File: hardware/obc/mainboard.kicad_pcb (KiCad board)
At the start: 6 copper layers, 95.9 x 90.2 mm, 216 parts, among them J101 Conn_02x20_Odd_Even, J301 USB_C_Receptacle_USB2.0, J302 Conn_High-Rel_4S2P_Vertical, J303 Conn_01x06, J304 Conn_High-Rel_6P, J305 Conn_01x05, J601 Conn_01x08_Socket, J602 SMA RA Connector, J603 SMA RA Connector, J604 SMA RA Connector, Q201 BSS138DWQ-7, Q202 BSS138DWQ-7, Q203 MBT2222ADW1T1, Q204 MBT2222ADW1T1, Q205 BSS138DWQ-7, Q206 BSS138DWQ-7, Q207 MBT2222ADW1T1, Q208 MBT2222ADW1T1, Q209 MMDT2907, Q401 MBT2222ADW1T1, Q402 MBT2222ADW1T1, Q403 IRLML2803, Q404 IRF7406PbF, Q501 MMBT2222AT, Q502 IRLML2803, Q503 IRLML2803, Q504 IRLML2803, Q505 IRF7406PbF, Q506 IRF7406PbF, Q507 IRF7406PbF, U101 MAX706RESA, U102 ATSAMD51J20A-AU, U103 BMI088, U301 Mem_MT29F4G01ABAFDWB, U302 Mem_MT29F4G01ABAFDWB, U401 TPS7A4501DCQT, U402 LTC4121, U403 TPS54226PWPRPWP14_2P31X2P46-L, U404 ADM1176-1ARMZ-R7, U405 BQ25886RGER, U501 PE014006, U601 RFM98PW, U602 S1216V8, U603 GP2S1+, Y101 32.768kHz

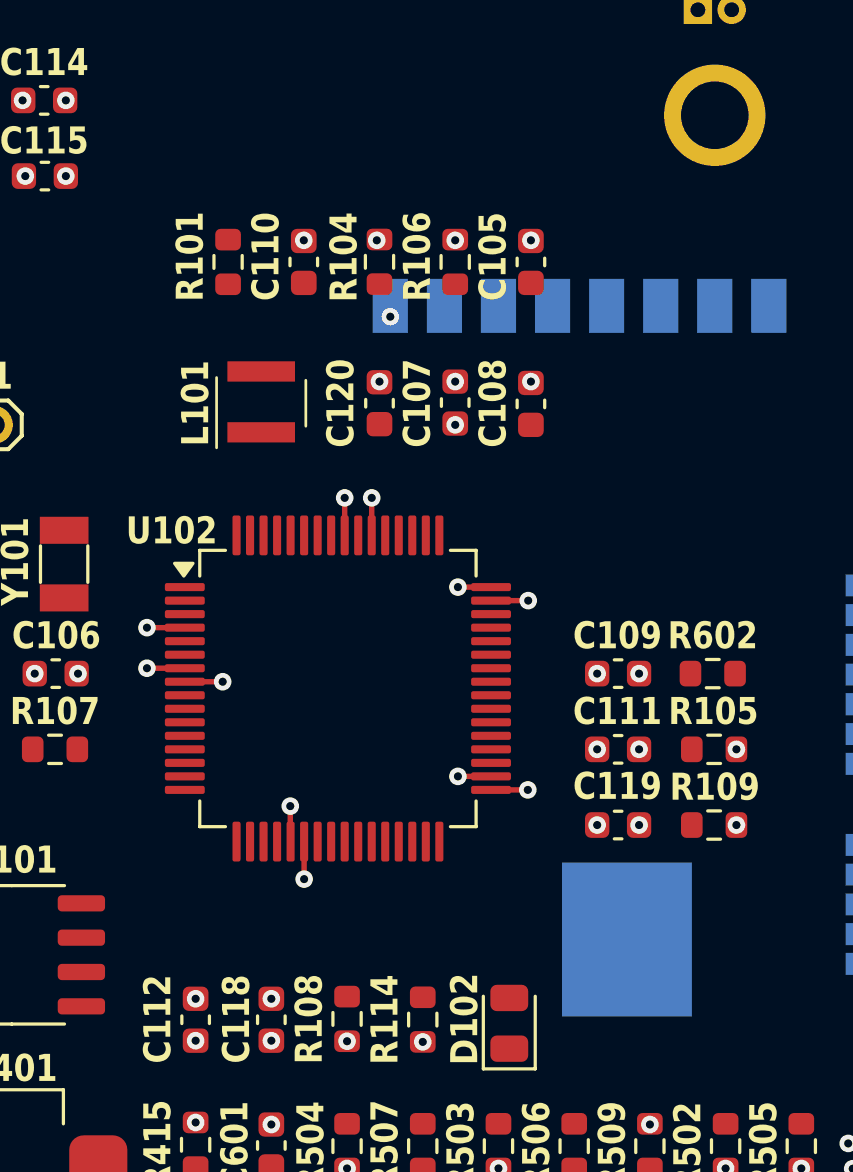
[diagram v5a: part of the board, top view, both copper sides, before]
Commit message: obc: slight adjustments
Edited radio footprint and added thick pwr trace to connect vburna on relay to pour. Slight adjustments to via centering.
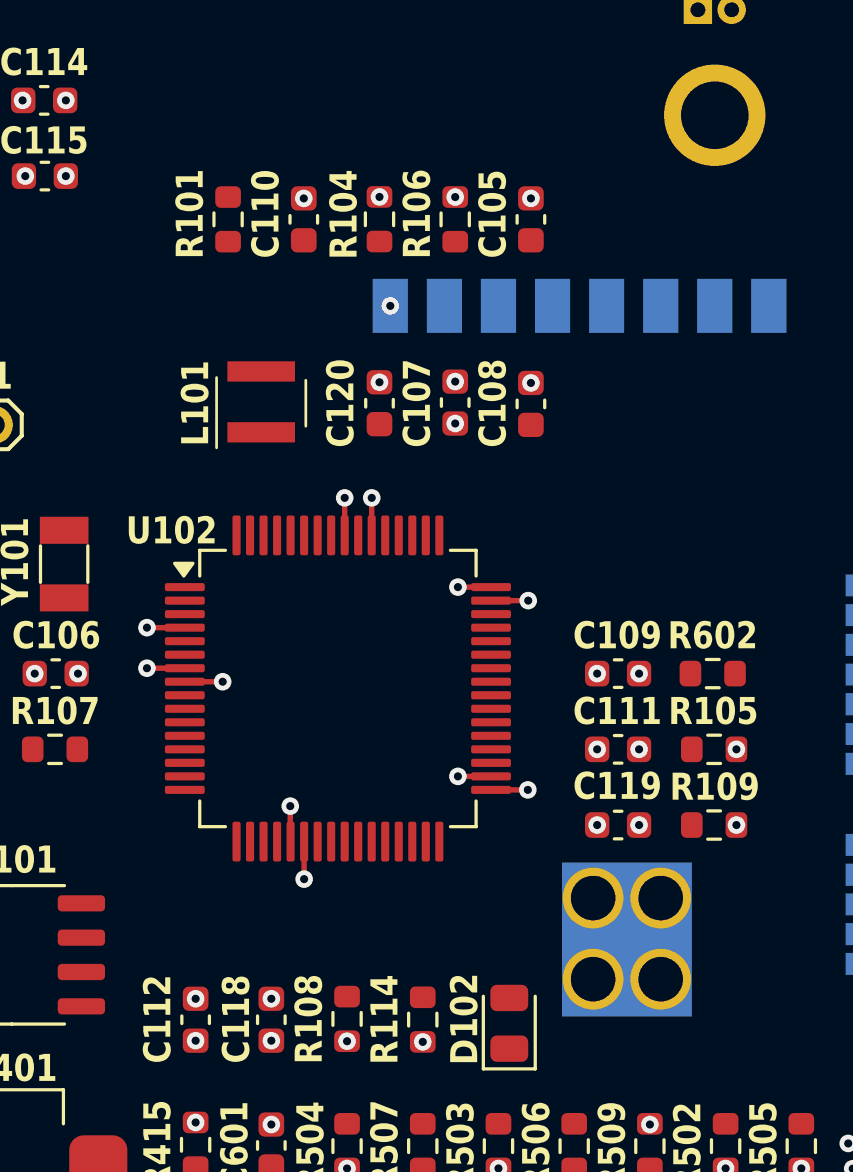
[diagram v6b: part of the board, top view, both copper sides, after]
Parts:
- moved C105 1.58 mm to (157.6, 84.3)
- moved C110 1.58 mm to (149.2, 84.3)
- moved R101 1.58 mm to (146.4, 84.3)
- moved R104 1.58 mm to (152.0, 84.3)
- moved R106 1.58 mm to (154.8, 84.3)
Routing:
- net /Burn Wires/VBURN_A_IN: track 0.00 -> 13.0 mm
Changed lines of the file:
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@@
 		)
 		(property "Value" "32.768kHz"
-			(at 0 2 -90)
+			(at 0 1.6625 -90)
 			(layer "F.Fab")
 			(effects
@@
 	(footprint "Resistor_SMD:R_0603_1608Metric"
 		(layer "F.Cu")
-		(at 152 85.87 -90)
+		(at 152 84.295 -90)
 		(descr "Resistor SMD 0603 (1608 Metric), square (rectangular) end terminal, IPC_7351 nominal, (Body size source: IPC-SM-782 page 72, https://www.pcb-3d.com/wordpress/wp-content/uploads/ipc-sm-782a_amendment_1_and_2.pdf), generated with kicad-footprint-generator")
 		(tags "resistor")
@@
 	(footprint "Resistor_SMD:R_0603_1608Metric"
 		(layer "F.Cu")
-		(at 146.4 85.875 90)
+		(at 146.4 84.3 90)
 		(descr "Resistor SMD 0603 (1608 Metric), square (rectangular) end terminal, IPC_7351 nominal, (Body size source: IPC-SM-782 page 72, https://www.pcb-3d.com/wordpress/wp-content/uploads/ipc-sm-782a_amendment_1_and_2.pdf), generated with kicad-footprint-generator")
 		(tags "resistor")
@@
 	(footprint "Capacitor_SMD:C_0603_1608Metric"
 		(layer "F.Cu")
-		(at 157.6 85.875 -90)
+		(at 157.6 84.3 -90)
 		(descr "Capacitor SMD 0603 (1608 Metric), square (rectangular) end terminal, IPC_7351 nominal, (Body size source: IPC-SM-782 page 76, https://www.pcb-3d.com/wordpress/wp-content/uploads/ipc-sm-782a_amendment_1_and_2.pdf), generated with kicad-footprint-generator")
 		(tags "capacitor")
@@
 	(footprint "Capacitor_SMD:C_0603_1608Metric"
 		(layer "F.Cu")
-		(at 149.2 85.875 90)
+		(at 149.2 84.3 90)
 		(descr "Capacitor SMD 0603 (1608 Metric), square (rectangular) end terminal, IPC_7351 nominal, (Body size source: IPC-SM-782 page 76, https://www.pcb-3d.com/wordpress/wp-content/uploads/ipc-sm-782a_amendment_1_and_2.pdf), generated with kicad-footprint-generator")
 		(tags "capacitor")
@@
 		(tags "resistor")
 		(property "Reference" "R112"
-			(at 0 -1.4 270)
+			(at 0 -1.4 -90)
 			(layer "F.SilkS")
 			(effects
@@
 		)
 		(property "Value" "DNI"
-			(at 0 1.43 270)
+			(at 0 1.43 -90)
 			(layer "F.Fab")
 			(effects
@@
 		)
 		(fp_text user "${REFERENCE}"
-			(at 0 0 270)
+			(at 0 0 -90)
 			(layer "F.Fab")
 			(effects
@@
 	(footprint "Resistor_SMD:R_0603_1608Metric"
 		(layer "F.Cu")
-		(at 154.8 85.875 -90)
+		(at 154.8 84.3 -90)
 		(descr "Resistor SMD 0603 (1608 Metric), square (rectangular) end terminal, IPC_7351 nominal, (Body size source: IPC-SM-782 page 72, https://www.pcb-3d.com/wordpress/wp-content/uploads/ipc-sm-782a_amendment_1_and_2.pdf), generated with kicad-footprint-generator")
 		(tags "resistor")
@@
 			)
 		)
-		(sheetname "RF and GPS")
-		(sheetfile "RF_and_GPS.kicad_sch")
 		(attr through_hole)
 		(fp_line
@@
 			)
 		)
+		(pad "" np_thru_hole circle
+			(at 4.5 -3.5 270)
+			(size 2.25 2.25)
+			(drill 1.65)
+			(layers "F&B.Cu" "*.Mask")
+		)
+		(pad "" np_thru_hole circle
+			(at 4.5 -1 270)
+			(size 2.25 2.25)
+			(drill 1.65)
+			(layers "F&B.Cu" "*.Mask")
+		)
+		(pad "" np_thru_hole circle
+			(at 7.5 -3.5 270)
+			(size 2.25 2.25)
+			(drill 1.65)
+			(layers "F&B.Cu" "*.Mask")
+		)
+		(pad "" np_thru_hole circle
+			(at 7.5 -1 270)
+			(size 2.25 2.25)
+			(drill 1.65)
+			(layers "F&B.Cu" "*.Mask")
+		)
 		(pad "1" smd rect
 			(at 17.6 -7.5 270)
@@
 	)
 	(via
-		(at 152 90.3)
+		(at 152 90.325)
 		(size 0.65)
 		(drill 0.3)
@@
 	)
 	(via
-		(at 157.6 85.075)
+		(at 157.6 83.525)
 		(size 0.65)
 		(drill 0.3)
@@
 	)
 	(via
-		(at 149.2 85.075)
+		(at 149.2 83.525)
 		(size 0.65)
 		(drill 0.3)
@@
 	)
 	(via
-		(at 157.6 90.3)
+		(at 157.6 90.35)
 		(size 0.65)
 		(drill 0.3)
@@
 	)
 	(via
-		(at 154.8 85.075)
+		(at 154.8 83.475)
 		(size 0.65)
 		(drill 0.3)
@@
 	)
 	(via
-		(at 152.4 87.9)
+		(at 152.4 87.5)
 		(size 0.65)
 		(drill 0.3)
@@
 	)
 	(via
-		(at 151.9 85.075)
+		(at 152 83.47)
 		(size 0.65)
 		(drill 0.3)
@@
 	)
 	(via
-		(at 154.8 91.9)
+		(at 154.8 91.85)
 		(size 0.65)
 		(drill 0.3)
@@
 		(net 120)
 	)
+	(segment
+		(start 132.8 123.1)
+		(end 142.4 123.1)
+		(width 2)
+		(layer "In1.Cu")
+		(net 120)
+	)
+	(segment
+		(start 131.735 124.165)
+		(end 132.8 123.1)
+		(width 2)
+		(layer "In1.Cu")
+		(net 120)
+	)
+	(segment
+		(start 131.735 126.09)
+		(end 131.735 124.165)
+		(width 2)
+		(layer "In1.Cu")
+		(net 120)
+	)
